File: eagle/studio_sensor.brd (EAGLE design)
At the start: 33 x 43.2 mm, 9 parts

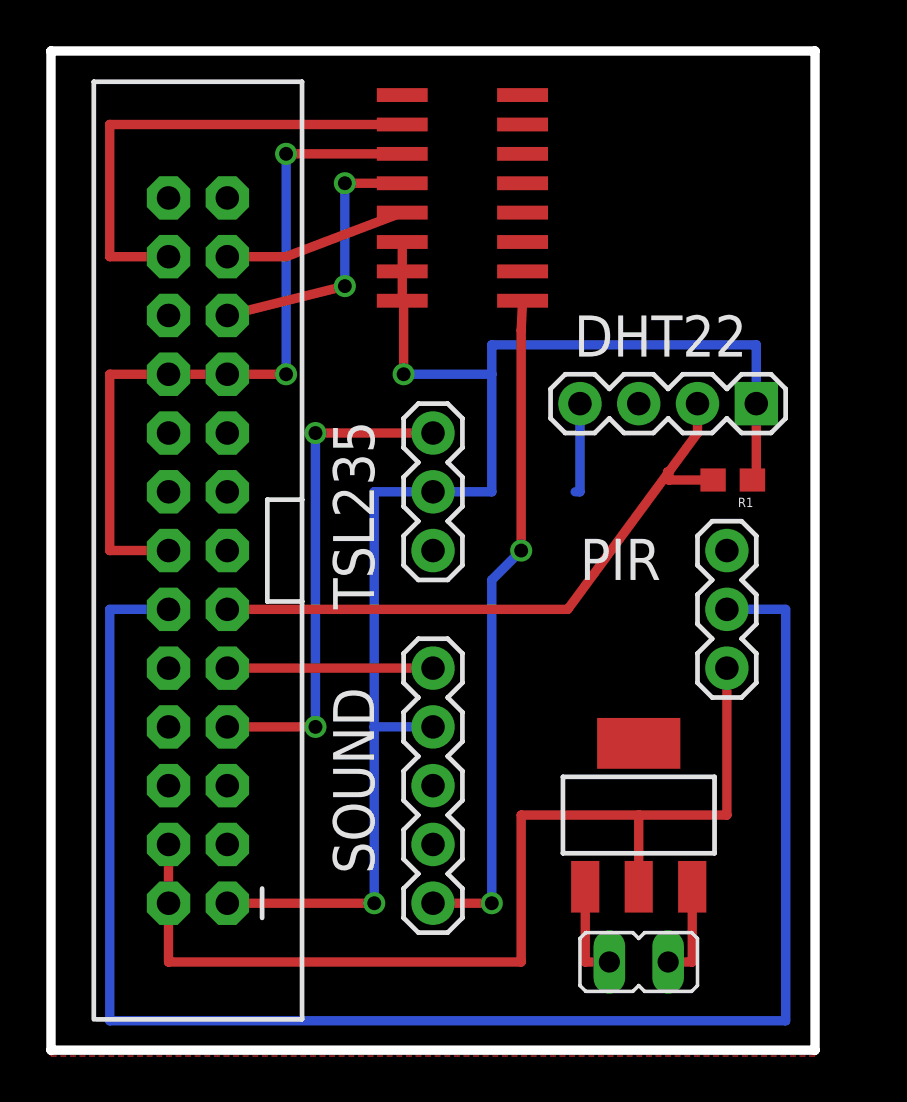
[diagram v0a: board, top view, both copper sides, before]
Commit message: updating studio sensors
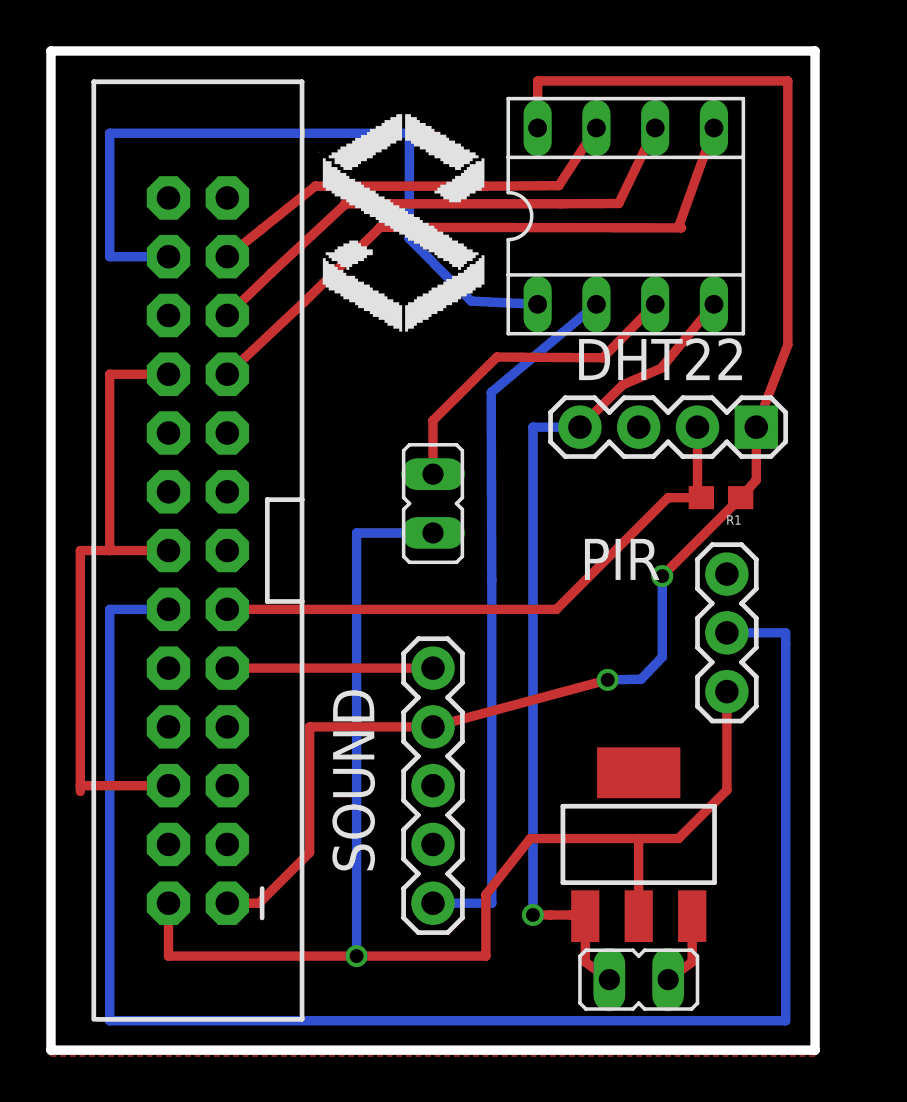
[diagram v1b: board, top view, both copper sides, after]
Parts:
- removed U$1: MCP3008SL, MCP3008:SO16
- added IC3: (no value), ic-package:SOCKET-08
- JP3: device SparkFun-Connectors:1X03 -> jumper:JP1
- moved JP3 2.03 mm to (16.5, 22.4), turned to 0 degrees
- moved IC1 1.27 mm to (25.4, 7.62)
- moved JP2 1.02 mm to (30.5, 25.7)
- moved JP4 1.02 mm to (29.2, 14.2)
- moved R1 0.92 mm to (29.0, 22.6)
- moved JP6 0.76 mm to (25.4, 1.78)
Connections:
- removed net N$14: JP1.7, JP3.3
- new net N$3: IC3.3, JP3.2
- net 5V: now also JP1.4; no longer JP1.2
- net GND: now also IC3.4; no longer JP3.1, U$1.9
- net N$1: now also JP1.2, JP3.1; no longer JP1.4
- net N$2: now also IC3.8; no longer JP3.2, U$1.14, U$1.15, U$1.16
- net N$4: now also IC3.7; no longer U$1.13
- net N$5: now also IC3.6; no longer U$1.12
- net N$6: now also IC3.5; no longer U$1.11
- net N$7: now also IC3.1; no longer U$1.10
- net N$8: now also IC3.2; no longer U$1.1
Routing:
- net GND: track 33.9 -> 73.6 mm, vias 0 -> 1
- net N$14: track 21.6 -> 0.00 mm, vias 2 -> 0
- net N$1: track 45.0 -> 60.3 mm, vias 0 -> 1
- net N$3: track 0.00 -> 14.0 mm
- net N$7: track 20.9 -> 32.1 mm
- net N$4: track 7.91 -> 18.4 mm
- net N$5: track 12.2 -> 22.5 mm, vias 2 -> 0
- net N$6: track 17.1 -> 26.8 mm, vias 2 -> 0
- net N$10: track 27.8 -> 25.7 mm
- net N$8: track 29.1 -> 30.5 mm, vias 2 -> 0
- net N$11: track 4.29 -> 3.27 mm
- net N$13: track 69.9 -> 68.8 mm
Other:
- board text removed: "TSL235"

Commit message: redoing DB
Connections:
- net GND: now also JP4.2; no longer JP4.3
- net N$13: now also JP4.3; no longer JP4.2
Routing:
- net N$13: track 68.8 -> 71.4 mm
- net N$2: track 65.5 -> 63.7 mm, vias 2 -> 0
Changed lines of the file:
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@@
 </polygon>
 <contactref element="JP1" pad="6"/>
-<contactref element="JP4" pad="3"/>
 <contactref element="IC1" pad="1"/>
 <contactref element="JP6" pad="2"/>
@@
 <wire x1="23.0886" y1="4.5212" x2="22.86" y2="4.5212" width="0.4064" layer="1"/>
 <wire x1="22.86" y1="4.5212" x2="22.86" y2="4.572" width="0.4064" layer="1"/>
-<wire x1="22.86" y1="4.572" x2="22.479" y2="4.572" width="0.4064" layer="1"/>
-<wire x1="22.479" y1="4.572" x2="21.59" y2="4.572" width="0.4064" layer="1"/>
+<wire x1="22.86" y1="4.572" x2="20.955" y2="4.572" width="0.4064" layer="1"/>
 <contactref element="JP5" pad="1"/>
 <contactref element="JP2" pad="4"/>
 <contactref element="IC3" pad="4"/>
-<wire x1="21.59" y1="4.572" x2="20.955" y2="4.572" width="0.4064" layer="1"/>
 <wire x1="22.86" y1="25.654" x2="20.828" y2="25.654" width="0.4064" layer="16"/>
 <wire x1="20.828" y1="25.654" x2="20.828" y2="4.572" width="0.4064" layer="16"/>
 <wire x1="7.62" y1="15.24" x2="16.51" y2="15.24" width="0.4064" layer="1"/>
 <wire x1="5.08" y1="10.16" x2="1.27" y2="10.16" width="0.4064" layer="1"/>
-<wire x1="1.27" y1="10.16" x2="1.27" y2="9.906" width="0.4064" layer="1"/>
-<wire x1="1.27" y1="10.16" x2="1.27" y2="20.32" width="0.4064" layer="1"/>
+<wire x1="1.27" y1="10.16" x2="1.27" y2="10.795" width="0.4064" layer="1"/>
+<wire x1="1.27" y1="10.795" x2="1.27" y2="20.32" width="0.4064" layer="1"/>
 <wire x1="1.27" y1="20.32" x2="2.54" y2="20.32" width="0.4064" layer="1"/>
 <wire x1="28.6512" y1="30.9626" x2="26.3652" y2="28.194" width="0.4064" layer="1"/>
@@
 <wire x1="24.7142" y1="27.4828" x2="22.86" y2="25.654" width="0.4064" layer="1"/>
 <via x="20.828" y="4.572" extent="1-16" drill="0.6" shape="square"/>
+<contactref element="JP4" pad="2"/>
 </signal>
 <signal name="3.3V">
@@
 <wire x1="7.62" y1="5.08" x2="8.9910125" y2="5.08" width="0.4064" layer="1"/>
 <wire x1="8.9910125" y1="5.08" x2="11.176" y2="7.2649875" width="0.4064" layer="1"/>
-<wire x1="11.176" y1="7.2649875" x2="11.176" y2="12.7" width="0.4064" layer="1"/>
-<wire x1="11.176" y1="12.7" x2="16.51" y2="12.7" width="0.4064" layer="1"/>
-<wire x1="16.51" y1="12.7" x2="24.058853125" y2="14.732" width="0.4064" layer="1"/>
-<wire x1="24.058853125" y1="14.732" x2="25.5028375" y2="14.758240625" width="0.4064" layer="16"/>
-<wire x1="25.5028375" y1="14.758240625" x2="26.416" y2="15.717175" width="0.4064" layer="16"/>
-<wire x1="26.416" y1="15.717175" x2="26.416" y2="19.216" width="0.4064" layer="16"/>
-<wire x1="26.416" y1="19.216" x2="29.806" y2="22.606" width="0.4064" layer="1"/>
-<via x="24.058853125" y="14.732" extent="1-16" drill="0.6" shape="square"/>
-<via x="26.416" y="19.216" extent="1-16" drill="0.6" shape="square"/>
+<wire x1="11.176" y1="7.2649875" x2="11.176" y2="9.914675" width="0.4064" layer="1"/>
+<wire x1="11.176" y1="9.914675" x2="13.961325" y2="12.7" width="0.4064" layer="1"/>
+<wire x1="13.961325" y1="12.7" x2="16.51" y2="12.7" width="0.4064" layer="1"/>
+<wire x1="16.51" y1="12.7" x2="21.899853125" y2="12.7" width="0.4064" layer="1"/>
+<wire x1="21.899853125" y1="12.7" x2="23.9788375" y2="14.758240625" width="0.4064" layer="1"/>
+<wire x1="23.9788375" y1="14.758240625" x2="24.003" y2="16.860175" width="0.4064" layer="1"/>
+<wire x1="24.003" y1="16.860175" x2="29.845" y2="22.645" width="0.4064" layer="1"/>
+<wire x1="29.845" y1="22.645" x2="29.806" y2="22.606" width="0.4064" layer="1"/>
 </signal>
 <signal name="N$13">
 <contactref element="JP1" pad="12"/>
-<wire x1="31.75" y1="16.256" x2="31.75" y2="0" width="0.4064" layer="16"/>
+<wire x1="31.75" y1="16.764" x2="31.75" y2="0" width="0.4064" layer="16"/>
 <wire x1="31.75" y1="0" x2="2.54" y2="0" width="0.4064" layer="16"/>
 <wire x1="2.54" y1="0" x2="2.54" y2="17.78" width="0.4064" layer="16"/>
 <wire x1="2.54" y1="17.78" x2="5.08" y2="17.78" width="0.4064" layer="16"/>
-<contactref element="JP4" pad="2"/>
-<wire x1="29.21" y1="16.764" x2="31.75" y2="16.764" width="0.4064" layer="16"/>
-<wire x1="31.75" y1="16.764" x2="31.75" y2="16.256" width="0.4064" layer="16"/>
+<contactref element="JP4" pad="3"/>
+<wire x1="29.21" y1="19.304" x2="31.75" y2="19.304" width="0.4064" layer="16"/>
+<wire x1="31.75" y1="19.304" x2="31.75" y2="16.764" width="0.4064" layer="16"/>
 </signal>
 <signal name="N$8">

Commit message: server updates
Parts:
- added C1: (no value), SparkFun-Capacitors:0603-CAP
- added J1: POWER_JACKPTH, SparkFun-Connectors:POWER_JACK_PTH
- JP6: device jumper:JP1 -> jumper:JP2
- moved IC1 11.9 mm to (13.7, 5.33)
- moved JP6 9.08 mm to (19.3, 8.51)
- moved JP5 7.05 mm to (14.9, 22.1)
- moved JP3 4.71 mm to (16.1, 27.1)
- moved R1 3.26 mm to (25.9, 21.5)
- moved JP4 2.19 mm to (29.6, 16.4)
- moved JP1 1.14 mm to (5.21, 20.3)
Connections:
- new net N$11: C1.2, J1.PWR
- new net N$12: C1.1, JP6.2
- net GND: now also J1.GND; no longer JP6.2
- net N$1: now also JP6.3, R1.2
- net N$10: no longer R1.2
- net N$13: now also R1.1
- net N$2: no longer R1.1
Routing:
- net GND: track 73.4 -> 48.4 mm, vias 1 -> 0
- net N$1: track 60.3 -> 73.9 mm
- net N$8: track 30.5 -> 22.9 mm
- net N$12: track 0.00 -> 6.64 mm
- net N$11: track 0.00 -> 5.53 mm
- net N$7: track 32.1 -> 26.7 mm
- net N$3: track 14.0 -> 10.9 mm
- net N$13: track 71.4 -> 69.0 mm
- net N$9: track 3.27 -> 5.26 mm
- net N$2: track 63.7 -> 65.6 mm
- net N$4: track 18.4 -> 19.1 mm
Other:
- board size 33 x 43.2 mm -> 34.8 x 43.2 mm
- board text added: "LIGHT"
